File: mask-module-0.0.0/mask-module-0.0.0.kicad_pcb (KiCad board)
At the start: 2 copper layers, 17.8 x 33 mm, 9 parts, among them J1 Conn_01x02, J2 USB_C_Receptacle_USB2.0, J3 Conn_01x13, J4 Conn_01x13, U1 BQ24075RGT, U2 BMD-340, U3 MCP1703Ax-330xxTT

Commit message: mask-module-0.0.0: update schematic
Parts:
- added C1: 1uF, Capacitor_SMD:C_0402_1005Metric, F.Cu at (43.0, 75.2)
- added C2: 4.7uF, Capacitor_SMD:C_0603_1608Metric, F.Cu at (43.3, 84.4)
- added C3: 4.7uF, Capacitor_SMD:C_0603_1608Metric, F.Cu at (41.5, 84.8)
- added C4: 4.7uF, Capacitor_SMD:C_0603_1608Metric, F.Cu at (45.5, 84.8)
- added C5: 4.7uF, Capacitor_SMD:C_0603_1608Metric, F.Cu at (47.2, 78.5)
- added C6: 4.7uF, Capacitor_SMD:C_0603_1608Metric, F.Cu at (43.9, 72.5)
- added C7: 1uF, Capacitor_SMD:C_0402_1005Metric, F.Cu at (37.9, 74.7)
- added C8: 1uF, Capacitor_SMD:C_0402_1005Metric, F.Cu at (37.9, 72.6)
- added D1: LED_Small, LED_SMD:LED_0402_1005Metric, F.Cu at (47.1, 72.3)
- added J3: Conn_ARM_JTAG_SWD_10, Connector:Tag-Connect_TC2050-IDC-NL_2x05_P1.27mm_Vertical, B.Cu at (43.2, 82.0)
- added J4: Conn_01x02, Connector_Molex:Molex_PicoBlade_53261-0271_1x02-1MP_P1.25mm_Horizontal, F.Cu at (72.3, 82.5)
- added R3: 10k, Resistor_SMD:R_0402_1005Metric, F.Cu at (44.5, 78.3)
- added R4: 10k, Resistor_SMD:R_0402_1005Metric, F.Cu at (46.0, 72.3)
- added R5: 10k / 2k, Resistor_SMD:R_0402_1005Metric, F.Cu at (43.0, 77.1)
- J2: footprint Connector_USB:USB_C_Receptacle_JAE_DX07S016JA1R1500 -> mask:USB_C_Receptacle_GCT_USB4520-xx-x-A_16P_Horizontal
- R1, R2: value 5.11k -> 5.1k; footprint Resistor_SMD:R_0603_1608Metric -> Resistor_SMD:R_0402_1005Metric
- moved U3 37.4 mm to (40.2, 73.8), turned to -90 degrees
- moved R1 36.8 mm to (38.3, 70.4)
- moved U1 27.1 mm to (45.7, 75.5), turned to 90 degrees
- moved R2 25.2 mm to (48.3, 70.5), turned to 180 degrees
- moved U2 16.6 mm to (43.4, 104.2)
- moved J1 11.0 mm to (61.8, 73.4), turned to -90 degrees
- moved J2 1.32 mm to (43.2, 65.8)
- renumbered J3 to J5, J4 to J6
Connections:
- J5 pad 1: unconnected-(J3-Pad1) -> GND
- J5 pad 2: unconnected-(J3-Pad2) -> TXD
- J5 pad 3: unconnected-(J3-Pad3) -> RXD
- J5 pad 4: unconnected-(J3-Pad4) -> GND
- J5 pad 5: unconnected-(J3-Pad5) -> GND
- J6 pad 1: unconnected-(J4-Pad1) -> VBAT
- J6 pad 2: unconnected-(J4-Pad2) -> +5V
- J6 pad 3: unconnected-(J4-Pad3) -> GND
- J6 pad 4: unconnected-(J4-Pad4) -> RESET
- J6 pad 5: unconnected-(J4-Pad5) -> +3V3
- U1 pad 1: unconnected-(U1-Pad1) -> Net-(R3-Pad1)
- U1 pad 10: Net-(U1-Pad10) -> +5V
- U1 pad 11: Net-(U1-Pad10) -> +5V
- U1 pad 13: unconnected-(U1-Pad13) -> VBUS
- U1 pad 15: unconnected-(U1-Pad15) -> GND
- U1 pad 16: unconnected-(U1-Pad16) -> Net-(R5-Pad1)
- U1 pad 17: Net-(U1-Pad17) -> GND
- U1 pad 2: Net-(U1-Pad2) -> VBAT
- U1 pad 3: Net-(U1-Pad2) -> VBAT
- U1 pad 4: unconnected-(U1-Pad4) -> GND
- U1 pad 5: unconnected-(U1-Pad5) -> GND
- U1 pad 6: unconnected-(U1-Pad6) -> +5V
- U1 pad 8: Net-(U1-Pad17) -> GND
- U1 pad 9: unconnected-(U1-Pad9) -> Net-(D1-Pad1)
- U2 pad 1: unconnected-(U2-Pad1) -> GND
- U2 pad 16: unconnected-(U2-Pad16) -> GND
- U2 pad 17: unconnected-(U2-Pad17) -> VDD_NRF
- U2 pad 18: unconnected-(U2-Pad18) -> GND
- U2 pad 2: unconnected-(U2-Pad2) -> GND
- U2 pad 29: unconnected-(U2-Pad29) -> GND
- U2 pad 3: unconnected-(U2-Pad3) -> GND
- U2 pad 30: unconnected-(U2-Pad30) -> GND
- U2 pad 4: unconnected-(U2-Pad4) -> GND
- U2 pad 45: unconnected-(U2-Pad45) -> GND
- U2 pad 46: unconnected-(U2-Pad46) -> GND
- U2 pad 47: unconnected-(U2-Pad47) -> GND
- U2 pad 5: unconnected-(U2-Pad5) -> GND
- U2 pad 55: unconnected-(U2-Pad55) -> GND
- U2 pad 65: unconnected-(U2-Pad65) -> +5V
- U2 pad 66: unconnected-(U2-Pad66) -> VBUS
- U3 pad 1: unconnected-(U3-Pad1) -> GND
- U3 pad 2: unconnected-(U3-Pad2) -> +3V3
- U3 pad 3: unconnected-(U3-Pad3) -> +5V

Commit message: module-0.0.0: more shematic work
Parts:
- removed U2: BMD-340, ublox:BMD-340
- added C10: 1uF, Capacitor_SMD:C_0402_1005Metric, F.Cu at (38.3, 90.8)
- added C9: 1uF, Capacitor_SMD:C_0402_1005Metric, F.Cu at (38.3, 85.8)
- added U4: BMD-380, ublox:BMD-380, F.Cu at (44.8, 90.5)
- added Y1: FC-135 32.768KA-A5, Crystal:Crystal_SMD_MicroCrystal_CC7V-T1A-2Pin_3.2x1.5mm, F.Cu at (38.6, 88.3)
- moved J4 33.1 mm to (39.3, 80.1), turned to -90 degrees
- moved C3 5.93 mm to (47.4, 84.6)
- moved C2 4.30 mm to (47.4, 83.1), turned to 0 degrees
- moved C4 3.70 mm to (47.4, 81.6)
- moved J3 1.86 mm to (42.3, 80.4), turned to -90 degrees
- moved R4 0.68 mm to (46.6, 72.1)
- moved C1 0.68 mm to (43.6, 75.0)
- moved C5 0.68 mm to (47.8, 78.3)
- moved C6 0.68 mm to (44.5, 72.3)
- moved D1 0.68 mm to (47.7, 72.1)
- moved R3 0.68 mm to (45.1, 78.1)
- moved R5 0.68 mm to (43.6, 76.9)
- moved U1 0.68 mm to (46.3, 75.3)
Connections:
- J3 pad 1: unconnected-(J3-Pad1) -> VDD_NRF
- J3 pad 10: unconnected-(J3-Pad10) -> RESET
- J3 pad 2: unconnected-(J3-Pad2) -> SWDIO
- J3 pad 3: Net-(J3-Pad3) -> GND
- J3 pad 4: unconnected-(J3-Pad4) -> SWCLK
- J3 pad 5: Net-(J3-Pad3) -> GND
- J5 pad 10: unconnected-(J5-Pad10) -> P1.00
- J5 pad 11: unconnected-(J5-Pad11) -> P0.11
- J5 pad 12: unconnected-(J5-Pad12) -> P1.04
- J5 pad 13: unconnected-(J5-Pad13) -> P1.06
- J5 pad 2: TXD -> P0.06_TXD
- J5 pad 3: RXD -> P0.08_RXD
- J5 pad 6: unconnected-(J5-Pad6) -> P0.17
- J5 pad 7: unconnected-(J5-Pad7) -> P0.20
- J5 pad 8: unconnected-(J5-Pad8) -> P0.22
- J5 pad 9: unconnected-(J5-Pad9) -> P0.24
- J6 pad 10: unconnected-(J6-Pad10) -> P1.13
- J6 pad 11: unconnected-(J6-Pad11) -> P1.11
- J6 pad 12: unconnected-(J6-Pad12) -> P0.10
- J6 pad 13: unconnected-(J6-Pad13) -> P0.09
- J6 pad 6: unconnected-(J6-Pad6) -> P0.31
- J6 pad 7: unconnected-(J6-Pad7) -> P0.29
- J6 pad 8: unconnected-(J6-Pad8) -> P0.02
- J6 pad 9: unconnected-(J6-Pad9) -> P1.15

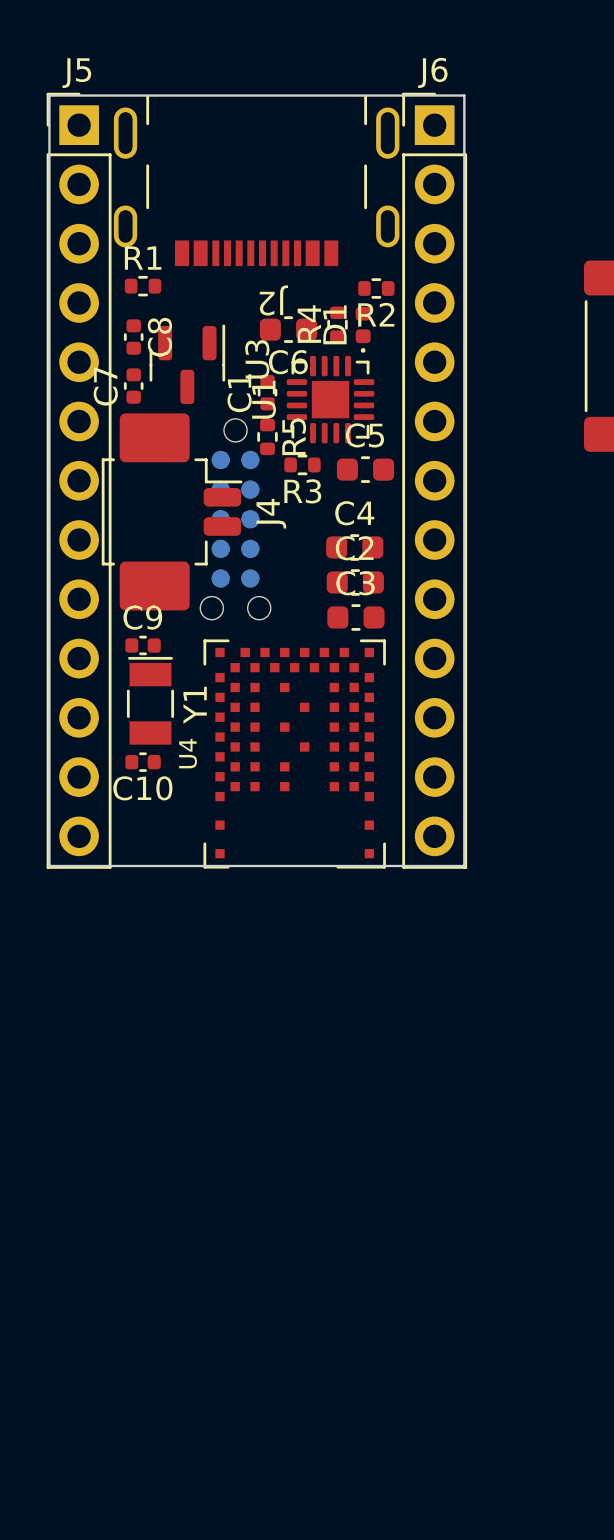
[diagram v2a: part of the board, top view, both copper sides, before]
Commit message: module-0.0.0: basic positioning
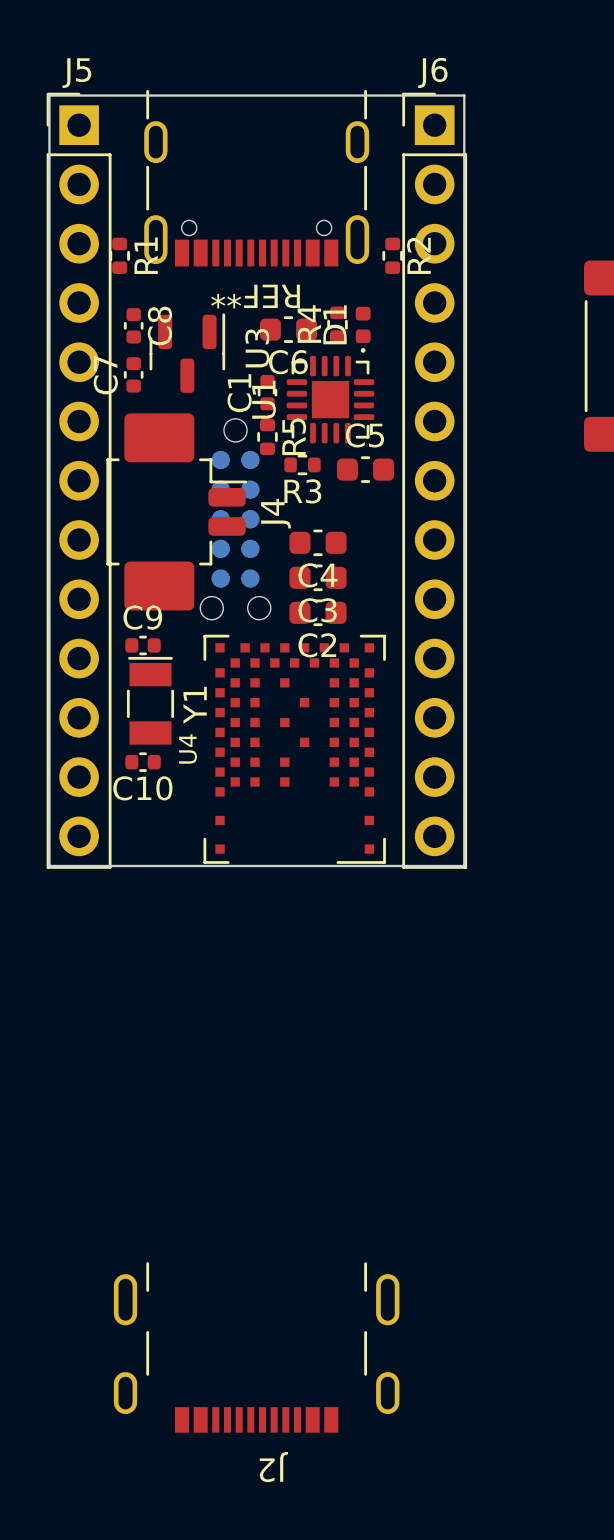
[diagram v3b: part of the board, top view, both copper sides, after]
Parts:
- added REF**: USB_C_Receptacle_GCT_USB4105-xx-A_16P_TopMnt_Horizontal, Connector_USB:USB_C_Receptacle_GCT_USB4105-xx-A_16P_TopMnt_Horizontal, F.Cu at (43.2, 65.3)
- moved J2 50.0 mm to (43.2, 115.8)
- moved C3 2.35 mm to (45.8, 82.9), turned to 180 degrees
- moved C2 2.06 mm to (45.8, 84.4), turned to 180 degrees
- moved R1 1.64 mm to (37.3, 69.1), turned to -90 degrees
- moved C4 1.59 mm to (45.8, 81.4), turned to 180 degrees
- moved R2 1.57 mm to (49.0, 69.1), turned to -90 degrees
- moved C7 0.48 mm to (37.9, 74.2)
- moved C8 0.48 mm to (37.9, 72.1)
- moved U3 0.48 mm to (40.2, 73.3)
- moved J4 0.20 mm to (39.5, 80.1)
- moved U4 0.20 mm to (44.8, 90.2)

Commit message: module-0.0.0: finish pcb
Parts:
- removed J1: Conn_01x02, Connector_JST:JST_PH_S2B-PH-SM4-TB_1x02-1MP_P2.00mm_Horizontal
- removed J4: Conn_01x02, Connector_Molex:Molex_PicoBlade_53261-0271_1x02-1MP_P1.25mm_Horizontal
- removed REF**: USB_C_Receptacle_GCT_USB4105-xx-A_16P_TopMnt_Horizontal, Connector_USB:USB_C_Receptacle_GCT_USB4105-xx-A_16P_TopMnt_Horizontal
- J2: footprint mask:USB_C_Receptacle_GCT_USB4520-xx-x-A_16P_Horizontal -> Connector_USB:USB_C_Receptacle_JAE_DX07S016JA1R1500
- moved R1 100.9 mm to (136.3, 88.7), turned to 0 degrees
- moved C7 100.1 mm to (136.5, 91.3)
- moved J2 99.3 mm to (137.2, 83.8)
- moved C8 98.2 mm to (133.6, 94.3), turned to 0 degrees
- moved C10 96.4 mm to (132.9, 109.4)
- moved C9 96.4 mm to (132.9, 104.3)
- moved Y1 96.4 mm to (133.2, 106.8)
- moved C2 96.2 mm to (140.3, 102.3)
- moved C3 96.2 mm to (140.3, 100.8)
- moved C4 96.2 mm to (140.3, 99.3)
- moved C6 95.8 mm to (138.6, 90.8)
- moved J5 95.8 mm to (129.6, 82.0)
- moved R4 95.8 mm to (140.7, 90.6)
- moved D1 95.8 mm to (141.8, 90.6)
- moved J3 95.8 mm to (136.3, 98.9)
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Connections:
- J5 pad 10: P1.00 -> P1.10
- J5 pad 11: P0.11 -> P1.06
- J5 pad 12: P1.04 -> P0.10
- J5 pad 13: P1.06 -> P0.09
- J5 pad 6: P0.17 -> P0.05
- J5 pad 7: P0.20 -> P0.27
- J5 pad 8: P0.22 -> P0.26
- J5 pad 9: P0.24 -> P0.04
- J6 pad 10: P1.13 -> P0.17
- J6 pad 11: P1.11 -> P0.21
- J6 pad 12: P0.10 -> P0.19
- J6 pad 13: P0.09 -> P0.22
- J6 pad 6: P0.31 -> P0.07
- J6 pad 7: P0.29 -> P0.12
- J6 pad 8: P0.02 -> P0.15
- J6 pad 9: P1.15 -> P0.14
- U4 pad 10: unconnected-(U4-P0.21-Pad10) -> P0.21
- U4 pad 16: unconnected-(U4-P0.14-Pad16) -> P0.14
- U4 pad 20: unconnected-(U4-P0.15-Pad20) -> P0.15
- U4 pad 26: unconnected-(U4-P0.12/TRACEDATA[1]-Pad26) -> P0.12
- U4 pad 27: unconnected-(U4-P0.07/TRACECLK-Pad27) -> P0.07
- U4 pad 31: unconnected-(U4-P0.05/AIN3-Pad31) -> P0.05
- U4 pad 32: unconnected-(U4-P0.27-Pad32) -> P0.27
- U4 pad 33: unconnected-(U4-P0.26-Pad33) -> P0.26
- U4 pad 34: unconnected-(U4-P0.04/AIN2-Pad34) -> P0.04
- U4 pad 49: unconnected-(U4-P1.10-Pad49) -> P1.10
- U4 pad 8: unconnected-(U4-P0.25-Pad8) -> P0.25
- U4 pad 9: unconnected-(U4-P0.19-Pad9) -> P0.19
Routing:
- net +5V: track 0.00 -> 41.6 mm, vias 0 -> 1
- net VBUS: track 0.00 -> 36.6 mm, vias 0 -> 4
- net RESET: track 0.00 -> 34.1 mm, vias 0 -> 2
- net D-: track 0.00 -> 29.4 mm, vias 0 -> 2
- net P0.06_TXD: track 0.00 -> 26.2 mm
- net D+: track 0.00 -> 25.8 mm, vias 0 -> 2
- net P0.08_RXD: track 0.00 -> 25.4 mm, vias 0 -> 1
- net +3V3: track 0.00 -> 21.0 mm, vias 0 -> 1
- net VBAT: track 0.00 -> 19.6 mm
- net SWDIO: track 0.00 -> 16.8 mm, vias 0 -> 1
- net P0.05: track 0.00 -> 16.6 mm
- net SWCLK: track 0.00 -> 14.9 mm, vias 0 -> 1
- net P0.07: track 0.00 -> 12.8 mm, vias 0 -> 2
- net P0.27: track 0.00 -> 12.3 mm
- net GND: track 0.00 -> 11.2 mm, vias 0 -> 38
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- added copper zone on B.Cu, net GND
- added copper zone on F.Cu, net GND
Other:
- board text removed: "InsightSIP ISP1807-LR-RS"
- board text removed: "ublox BMD-380"
